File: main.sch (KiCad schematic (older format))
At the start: 48 parts, among them J1 USB_OTG, J2 JTAG Port, J3 C Port, J4 A Port, J5 E Port, J6 D Port, J7 B Port, J8 F Port, SW1 SW_Push, SW2 SW_Push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

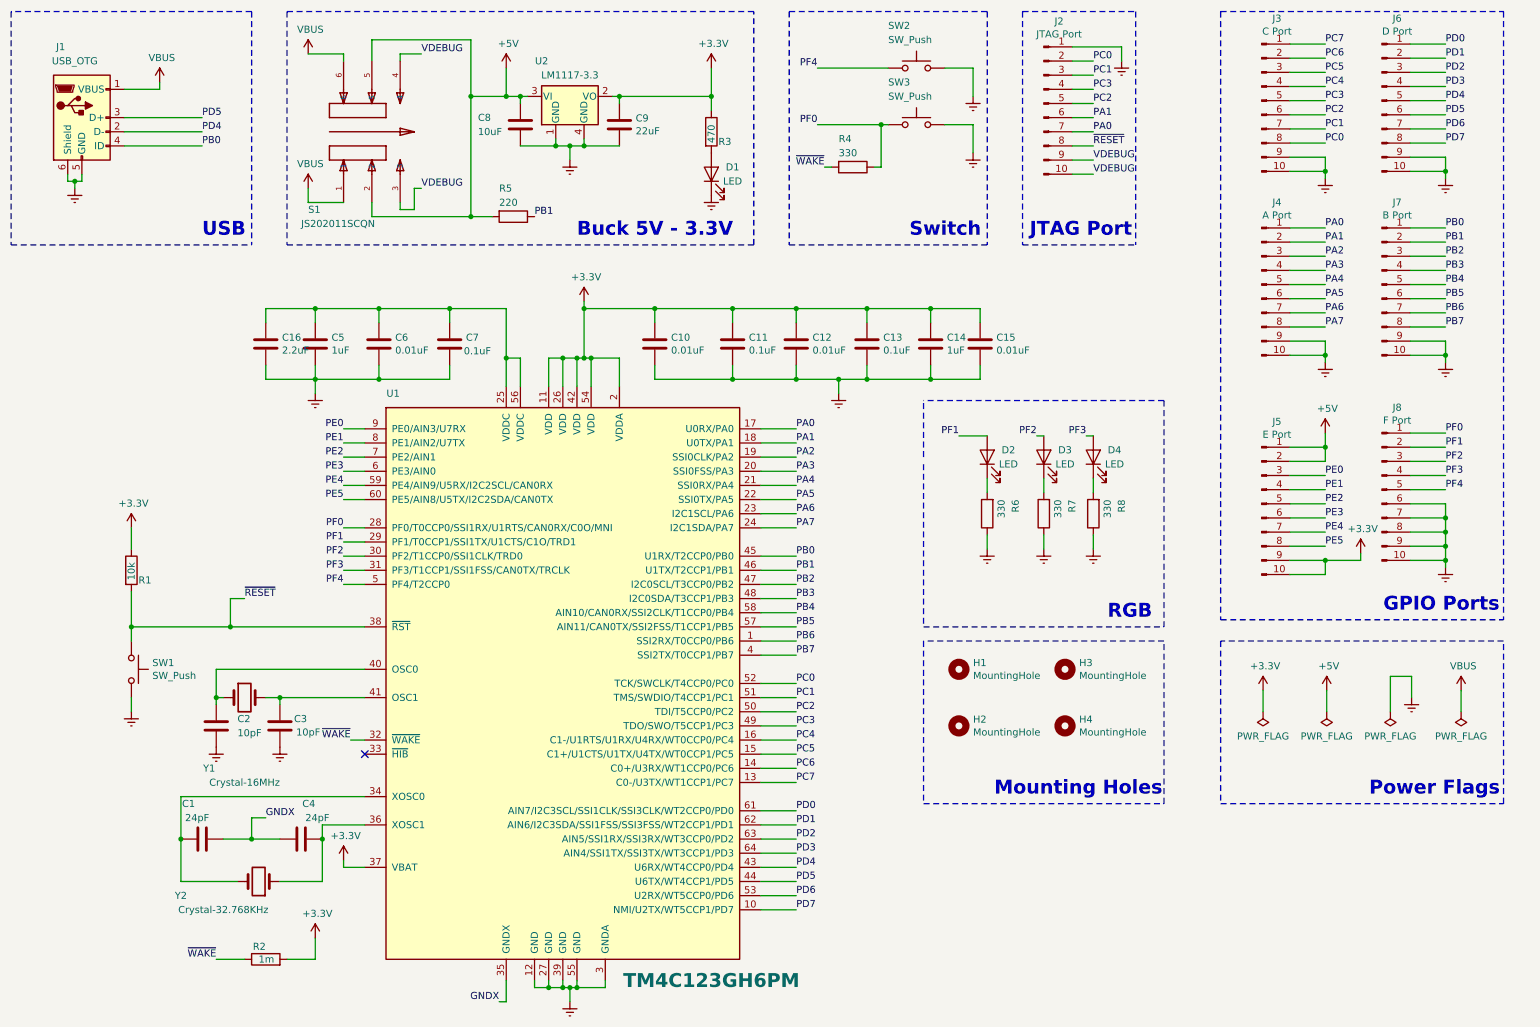
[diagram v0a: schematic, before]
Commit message: Updated
Cập nhật lại điện trở treo cho JTAG
Thay thạch anh SMD thành loại dễ tìm hơn
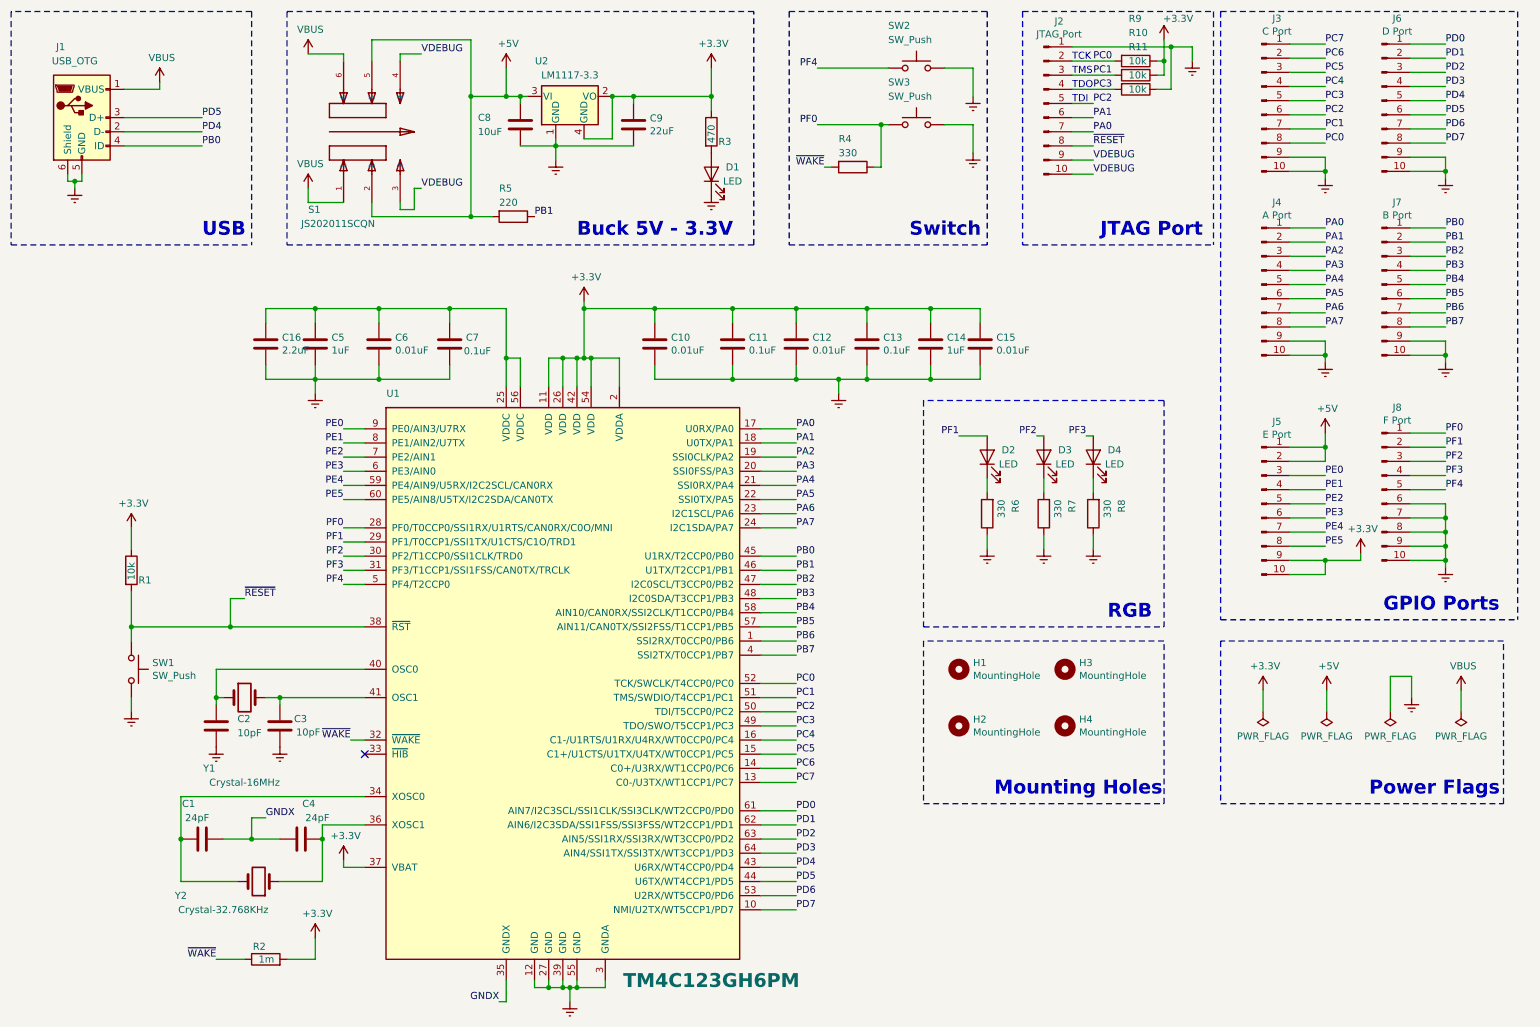
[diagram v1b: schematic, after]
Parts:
- added R10, R11, R9: 10k, tm4c:R_0805_2012Metric_Pad1.15x1.40mm_HandSolder, symbol Device:R
- Y1: footprint tm4c:Crystal_SMD_5032-2Pin_5.0x3.2mm_HandSoldering -> tm4c:Crystal_SMD_HC49-SD
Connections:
- net +3V3: now also U2.4 (GND), R10.1, R9.1
- net Earth: now also R11.1; no longer U2.4 (GND)
- net PC0: now also R9.2
- net PC1: now also R10.2
- net PC3: now also R11.2
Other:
- note added: "TCK"
- note added: "TDI"
- note added: "TDO"
- note added: "TMS"
- moved on the sheet: C9

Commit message: Updated a little
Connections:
- net Earth: now also J2.10 (Pin_10)
- net VDEBUG: no longer J2.10 (Pin_10)
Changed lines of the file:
@@
 Rev "1.2"
 Comp "Future Energy"
-Comment1 ""
-Comment2 ""
+Comment1 "TCK & TMS pull up with 10k Res"
+Comment2 "TD0 pull down with 10k Res"
 Comment3 ""
 Comment4 ""
@@
 	1    0    0    -1
 $EndComp
-Text Label 8200 1700 0    50   ~ 0
-VDEBUG
-Wire Wire Line
-	8050 1700 8200 1700
 $Comp
 L Device:R R5
@@
 	4800 1150 4800 1450
 Connection ~ 4800 1150
+$Comp
+L power:Earth #PWR037
+U 1 1 5E15E177
+P 8300 1750
+F 0 "#PWR037" H 8300 1500 50  0001 C CNN
+F 1 "Earth" H 8300 1600 50  0001 C CNN
+F 2 "" H 8300 1750 50  0001 C CNN
+F 3 "~" H 8300 1750 50  0001 C CNN
+	1    8300 1750
+	1    0    0    -1
+$EndComp
+Wire Wire Line
+	8300 1700 8300 1750
+Wire Wire Line
+	8050 1700 8300 1700
 $EndSCHEMATC

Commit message: Updated
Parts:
- SW2, SW3: symbol Switch:SW_Push -> tm4c:SW_Push
- U2: symbol tm4c:LM1117-3.3 -> tm4c:TLV1117-33
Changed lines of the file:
@@
 $EndComp
 $Comp
-L tm4c:LM1117-3.3 U?
+L tm4c:TLV1117-33 U?
 U 1 1 5DE9FDCD
 P 4500 1150
@@
 Connection ~ 4600 3000
 $Comp
-L Switch:SW_Push SW2
+L tm4c:SW_Push SW2
 U 1 1 5E8B83A0
 P 6950 950
@@
 	7350 950  7350 1150
 $Comp
-L Switch:SW_Push SW3
+L tm4c:SW_Push SW3
 U 1 1 5E8F2D13
 P 6950 1350
